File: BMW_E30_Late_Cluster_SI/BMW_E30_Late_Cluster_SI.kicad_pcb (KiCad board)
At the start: 2 copper layers, 300 x 53 mm, 115 parts, among them J1 SI LED Board, J2 Coding Plug, J5 Nexus Connector, Q11 BC327-16, Q12 BC337-25, Q13 BC337-16, Q14 BC547B, Q15 BC557B, Q17 BC337-25, Q19 BC337-25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

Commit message: Moved C17 for readability
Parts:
- R28: value 200R -> 200k

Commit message: Add SMD Provisions
Added SMD mount options for C12, C4, and C2 so that axial lead electrolytics are not necessary to purchase from the BOM.
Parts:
- added C12.1: 100u, Capacitor_SMD:CP_Elec_6.3x5.8, F.Cu at (222.5, 175.7)
- added C2.1: 100u, Capacitor_SMD:CP_Elec_6.3x5.8, F.Cu at (285.9, 134.8)
- added C4.1: 100u, Capacitor_SMD:CP_Elec_6.3x5.8, F.Cu at (287.4, 172.0)
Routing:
- net VCC_T15: track 458.8 -> 469.6 mm
- net Net-(Q17-C): track 303.7 -> 313.7 mm
- net VCC_T30: track 20.4 -> 26.8 mm
- net GNDPWR: track 777.0 -> 783.2 mm, vias 24 -> 26
- net IC1_P4: track 322.9 -> 324.1 mm, vias 1 -> 3
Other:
- board text added: "Late Model SI Board Revision: V1.2"

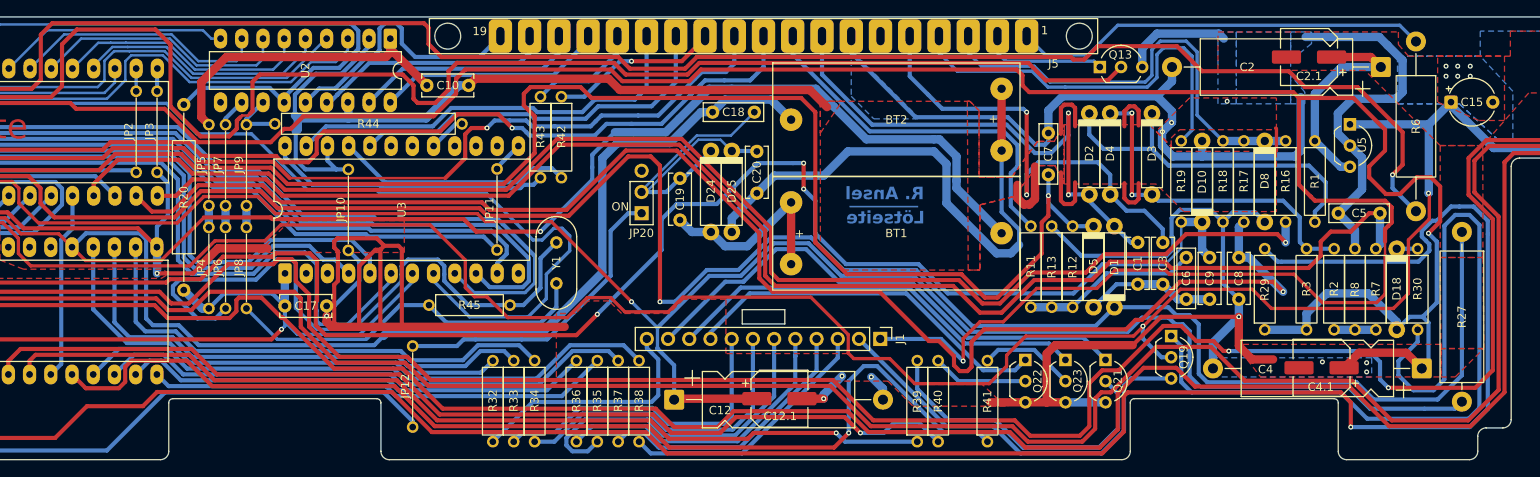
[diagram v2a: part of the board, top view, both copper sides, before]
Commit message: Layout Fitment Changes
Widened both bottom slots of the board size. Also shifted J5 and J1 to match the original board better. Anchor point is the coding plug insert. This offsets the original anchor point of the left board edge.
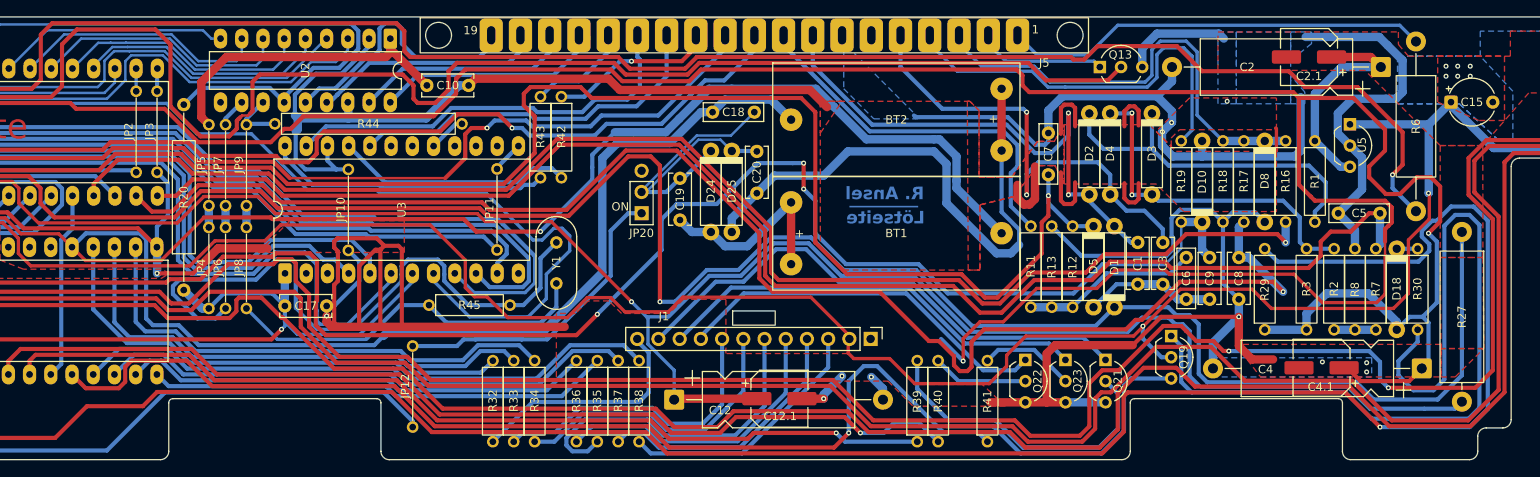
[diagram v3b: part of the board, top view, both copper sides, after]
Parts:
- J1: footprint Connector_PinHeader_2.54mm:PinHeader_1x12_P2.54mm_Vertical -> BMW_Cluster_Connectors:SILight_1x12_P2.54mm_Vertical_PinHeader
- moved J1 29.1 mm to (205.5, 168.6), turned to 0 degrees
- moved J5 1.10 mm to (219.5, 132.2)
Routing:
- net Net-(J1-Pin_2): track 49.9 -> 35.1 mm
- net GNDPWR: track 783.2 -> 770.9 mm
- net VCC_T15: track 469.6 -> 462.1 mm
- net Net-(J1-Pin_7): track 37.7 -> 35.3 mm
- net Fuel_rate_input: track 142.3 -> 140.1 mm
- net Wheel_spd_output: track 135.3 -> 133.2 mm
- net Net-(J1-Pin_8): track 38.1 -> 36.2 mm
- net Net-(JP1-B): track 288.7 -> 286.9 mm
- net EG_2-: track 45.7 -> 44.3 mm
- net Net-(J1-Pin_12): track 29.4 -> 28.1 mm
- net Net-(J1-Pin_10): track 51.2 -> 52.3 mm
- net Net-(J1-Pin_11): track 62.3 -> 63.5 mm
- net Temp_+Ub: track 49.8 -> 50.9 mm
- net Tach_2+: track 28.8 -> 27.6 mm
- net EG_1+: track 13.4 -> 12.3 mm
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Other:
- outline, holes or cut-outs redrawn

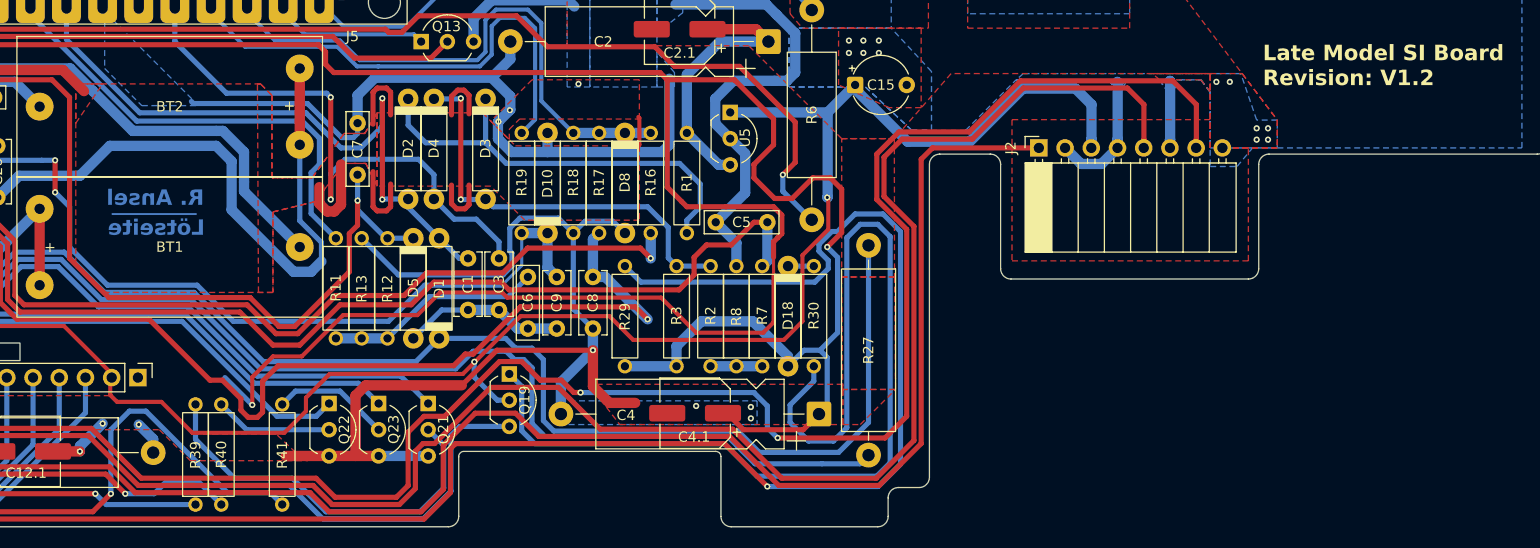
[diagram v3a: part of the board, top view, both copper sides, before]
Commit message: Layout fixes
Some traces were not connected.
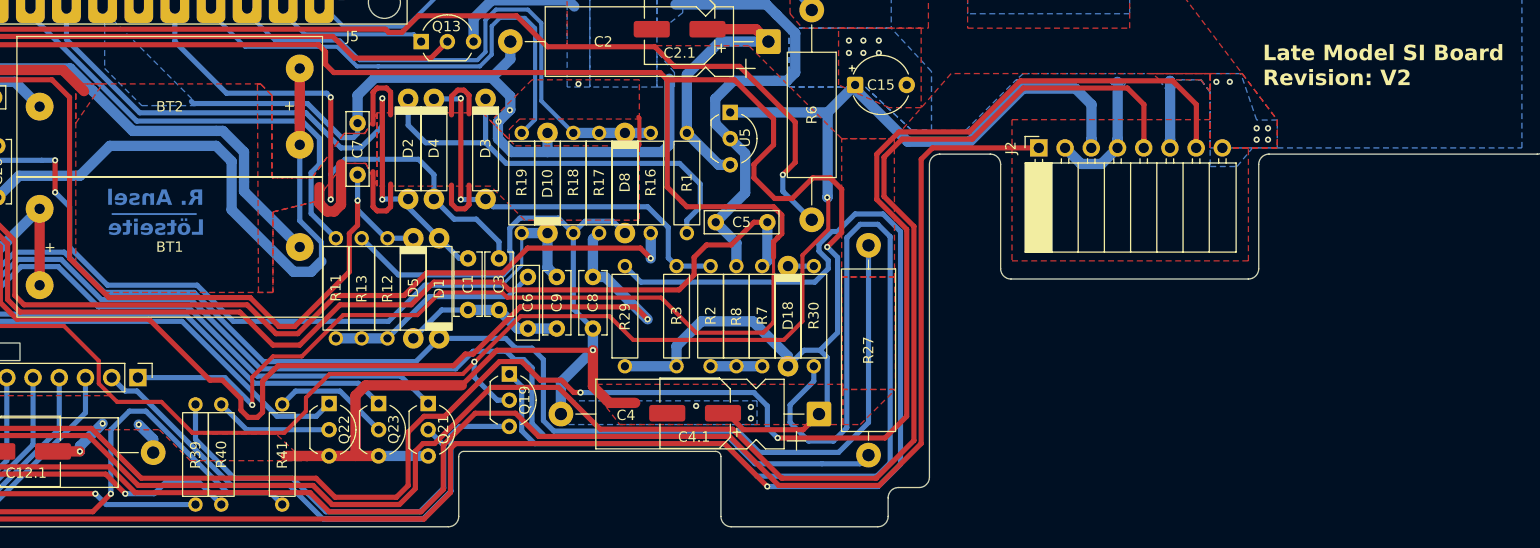
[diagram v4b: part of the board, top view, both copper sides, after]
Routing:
- net Net-(J1-Pin_2): track 35.1 -> 51.1 mm
- net VCC_T15: track 462.1 -> 470.5 mm
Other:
- board text added: "Late Model SI Board Revision: V2"
- board text removed: "Late Model SI Board Revision: V1.2"

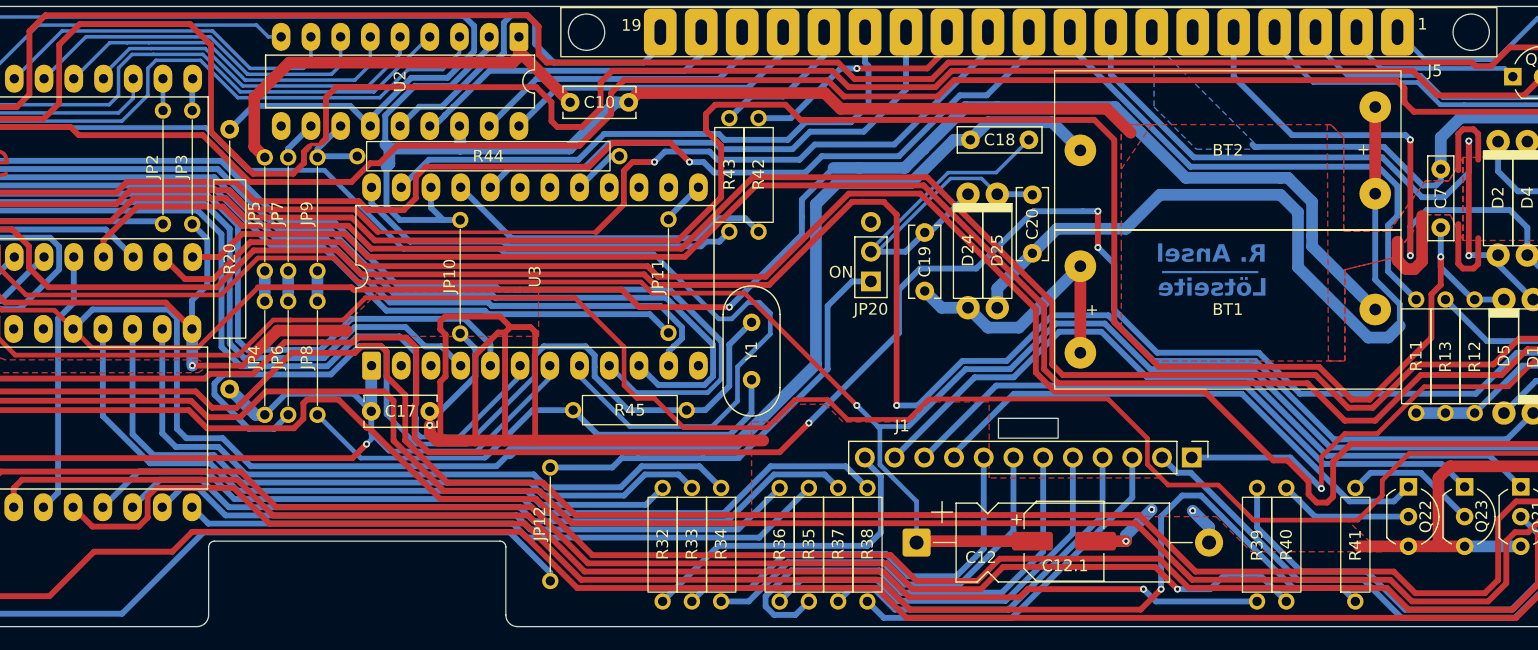
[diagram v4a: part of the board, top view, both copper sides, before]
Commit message: Layout Updates
Moved battery footprints to closer match the original. Also moved the groupings of resistors in the center lower section of the board to be further away from the board edge for better fitment.
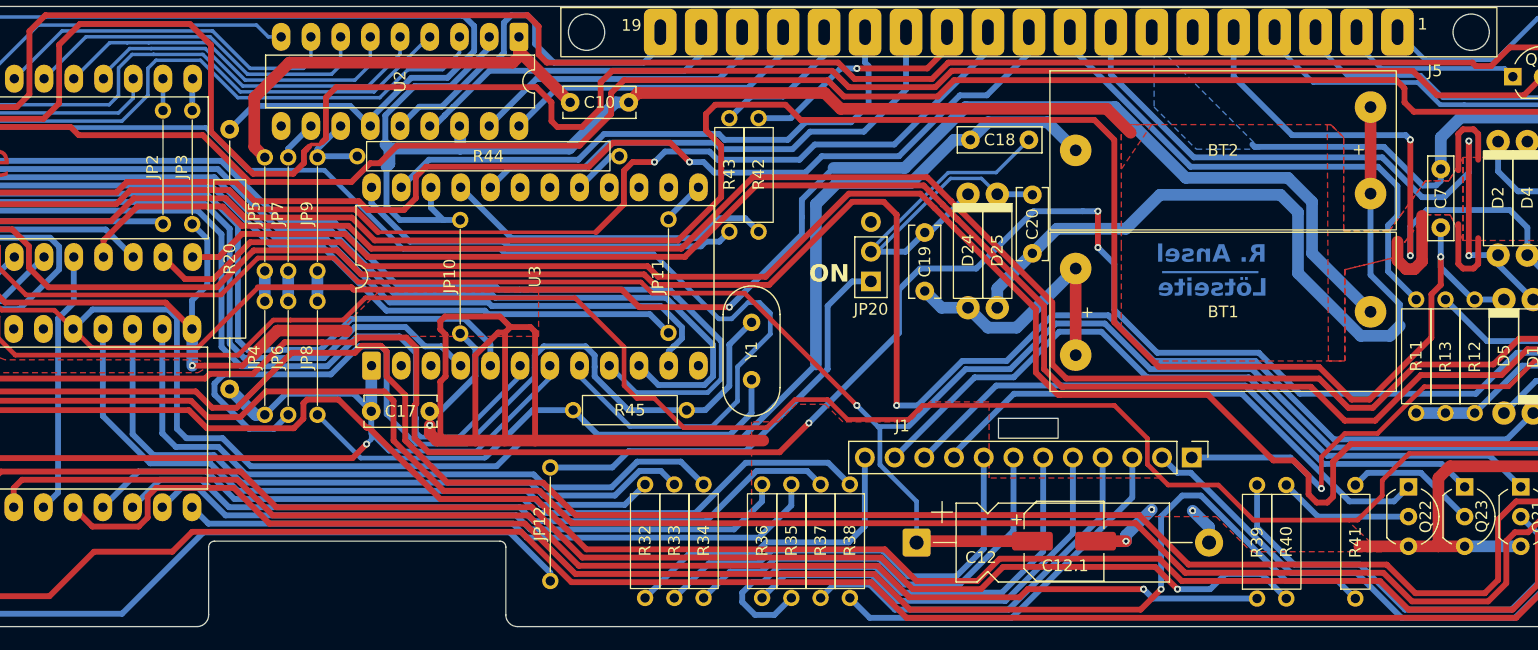
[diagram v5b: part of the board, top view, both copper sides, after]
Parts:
- moved R32 1.53 mm to (186.7, 170.8)
- moved R33 1.53 mm to (189.2, 170.8)
- moved R34 1.53 mm to (191.7, 170.8)
- moved R35 1.53 mm to (199.2, 170.8)
- moved R36 1.53 mm to (196.7, 170.8)
- moved R37 1.53 mm to (201.7, 170.8)
- moved R38 1.53 mm to (204.2, 170.8)
- moved BT1 0.45 mm to (236.1, 156.1)
- moved BT2 0.40 mm to (236.1, 142.3)
- moved R39 0.25 mm to (239.0, 180.6)
- moved R40 0.25 mm to (241.5, 180.6)
- moved R41 0.25 mm to (247.4, 180.6)
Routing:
- net Net-(J1-Pin_6): track 40.3 -> 43.1 mm
- net Net-(J1-Pin_5): track 35.4 -> 37.2 mm
- net Net-(J1-Pin_3): track 30.9 -> 32.5 mm
- net Net-(J1-Pin_4): track 32.1 -> 33.8 mm
- net Net-(J1-Pin_8): track 36.2 -> 37.8 mm
- net Net-(J1-Pin_7): track 35.3 -> 36.9 mm
- net IC4_P23: track 60.2 -> 58.8 mm
- net IC4_P18: track 64.9 -> 63.5 mm
- net IC4_P24: track 59.0 -> 57.6 mm
- net IC4_P17: track 70.5 -> 69.1 mm
- net IC4_P22: track 60.1 -> 58.8 mm
- net Net-(J1-Pin_12): track 28.1 -> 27.2 mm
- net IC4_P19: track 56.4 -> 55.9 mm
